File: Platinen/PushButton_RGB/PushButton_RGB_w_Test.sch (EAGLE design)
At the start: 149 parts, among them IC1 4017D, IC2 4011D, IC3 4017D

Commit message: First Version Push Button 16x RGB
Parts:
- LED1: device led:LED3MM -> led:LEDCHIPLED_0805
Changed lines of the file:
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@@
 <part name="GND6" library="supply1" library_urn="urn:adsk.eagle:library:371" deviceset="GND" device=""/>
 <part name="GND5" library="supply1" library_urn="urn:adsk.eagle:library:371" deviceset="GND" device=""/>
-<part name="LED1" library="led" library_urn="urn:adsk.eagle:library:259" deviceset="LED" device="3MM" package3d_urn="urn:adsk.eagle:package:15797/1" value="green"/>
+<part name="LED1" library="led" library_urn="urn:adsk.eagle:library:259" deviceset="LED" device="CHIPLED_0805" package3d_urn="urn:adsk.eagle:package:15821/2" value="green"/>
 <part name="R20" library="rcl" library_urn="urn:adsk.eagle:library:334" deviceset="R-EU_" device="R0603" package3d_urn="urn:adsk.eagle:package:23555/2" value="470"/>
 <part name="GND7" library="supply1" library_urn="urn:adsk.eagle:library:371" deviceset="GND" device=""/>
@@
 </instance>
 <instance part="TST_LED1" gate="G$1" x="365.76" y="218.44" smashed="yes" rot="MR90">
-<attribute name="VALUE" x="371.348" y="215.392" size="1.778" layer="96" rot="MR90"/>
 <attribute name="NAME" x="362.204" y="226.822" size="1.778" layer="95" rot="MR270"/>
 </instance>

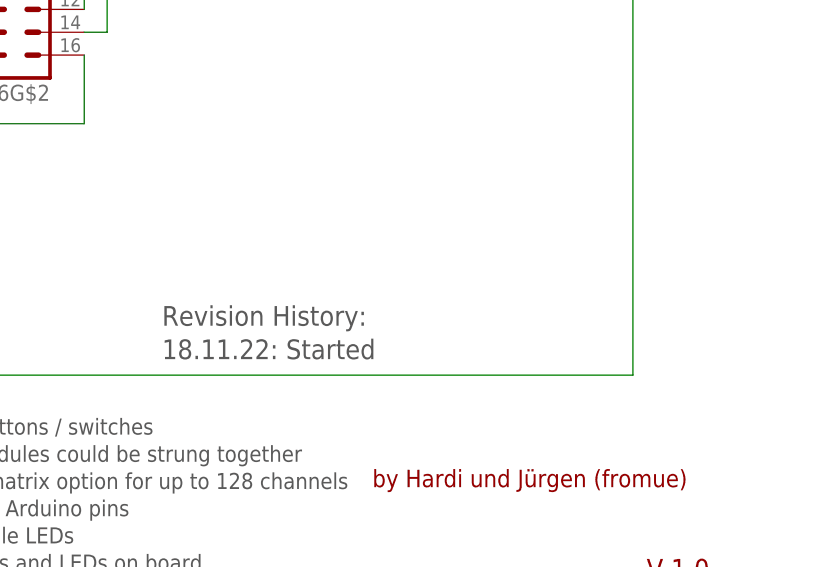
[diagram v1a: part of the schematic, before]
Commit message: Corrected placement of the diodes at the bottom
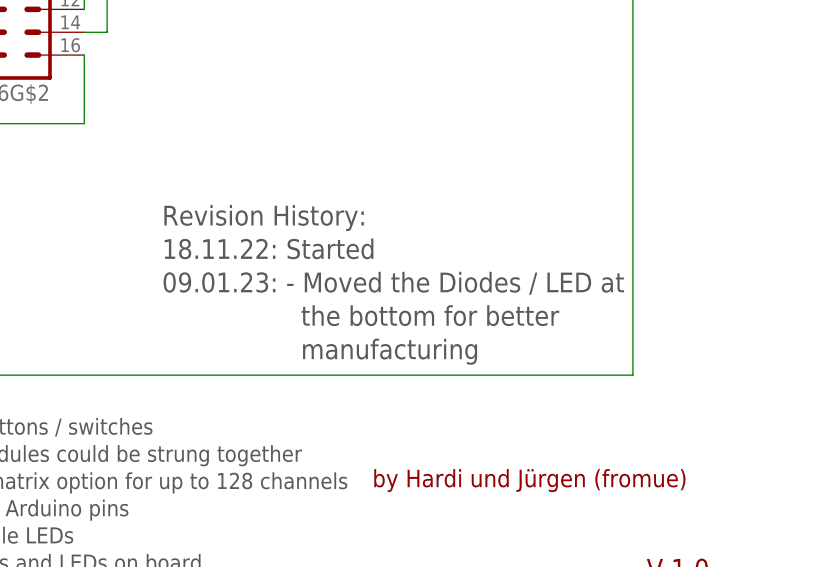
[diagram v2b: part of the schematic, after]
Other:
- note added: "Revision History: 18.11.22: Started 09.01.23: - Moved the Diodes / LED at the bottom for better manufacturing"
- note removed: "Revision History: 18.11.22: Started"
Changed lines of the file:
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@@
 a second string.</text>
 <text x="323.596" y="32.258" size="2.1844" layer="97" distance="70">Revision History:
-18.11.22: Started</text>
+18.11.22: Started
+09.01.23: - Moved the Diodes / LED at
+                  the bottom for better
+                  manufacturing </text>
 <text x="377.444" y="7.874" size="2.1844" layer="94">V 1.0</text>
 <text x="41.91" y="215.646" size="1.778" layer="97">Buttons:
